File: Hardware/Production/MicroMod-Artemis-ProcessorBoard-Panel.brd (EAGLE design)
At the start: 244.6 x 83.1 mm, 766 parts, among them J1 MICROMOD-2222, J10 MICROMOD-2222, J11 MICROMOD-2222, J12 MICROMOD-2222, J13 MICROMOD-2222, J14 MICROMOD-2222, J15 MICROMOD-2222, J16 MICROMOD-2222, J17 MICROMOD-2222, J18 MICROMOD-2222, J19 MICROMOD-2222, J2 MICROMOD-2222, J20 MICROMOD-2222, J3 MICROMOD-2222, J4 MICROMOD-2222, J5 MICROMOD-2222, J6 MICROMOD-2222, J7 MICROMOD-2222, J8 MICROMOD-2222, J9 MICROMOD-2222, U1 ARTEMIS_MODULESMD, U10 ARTEMIS_MODULESMD, U11 CH340E_MSOP10, U12 TSV524, U13 ARTEMIS_MODULESMD, U14 CH340E_MSOP10, U15 TSV524, U16 ARTEMIS_MODULESMD, U17 CH340E_MSOP10, U18 TSV524, U19 ARTEMIS_MODULESMD, U2 TSV524, U20 CH340E_MSOP10, U21 TSV524, U22 ARTEMIS_MODULESMD, U23 CH340E_MSOP10, U24 TSV524, U25 ARTEMIS_MODULESMD, U26 CH340E_MSOP10, U27 TSV524, U28 ARTEMIS_MODULESMD, U29 CH340E_MSOP10, U3 ARTEMIS_MODULESMD, U30 TSV524, U31 ARTEMIS_MODULESMD, U32 CH340E_MSOP10, U33 TSV524, U34 ARTEMIS_MODULESMD, U35 CH340E_MSOP10, U36 TSV524, U37 ARTEMIS_MODULESMD, U38 CH340E_MSOP10, U39 TSV524, U4 CH340E_MSOP10, U40 ARTEMIS_MODULESMD, U41 CH340E_MSOP10, U42 TSV524, U43 ARTEMIS_MODULESMD, U44 CH340E_MSOP10, U45 TSV524, U46 ARTEMIS_MODULESMD, U47 CH340E_MSOP10, U48 TSV524, U49 ARTEMIS_MODULESMD, U5 TSV524, U50 CH340E_MSOP10, U51 TSV524, U52 ARTEMIS_MODULESMD, U53 CH340E_MSOP10, U54 TSV524, U55 ARTEMIS_MODULESMD, U56 CH340E_MSOP10, U57 TSV524, U58 ARTEMIS_MODULESMD, U59 CH340E_MSOP10, U6 CH340E_MSOP10, U60 TSV524, U7 ARTEMIS_MODULESMD, U8 CH340E_MSOP10, U9 TSV524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

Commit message: Adding v13 production files
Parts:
- removed C129, C130, C137, C138, C145, C146, C153, C154: 15pF, SparkFun-Capacitors:0402-TIGHT
- removed C131, C139, C147, C155: 10nF, SparkFun-Capacitors:0402-TIGHT
- removed C132, C133, C134, C136, C140, C141, C142, C144, C148, C149, C150, C152, C156, C157, C158, C160: 0.1uF, SparkFun-Capacitors:0402-TIGHT
- removed C135, C143, C151, C159: 1.0nF, SparkFun-Capacitors:0402-TIGHT
- removed D33, D35, D37, D39: BLUE, SparkFun-LED:LED-0603
- removed D34, D36, D38, D40: 1A/23V/620mV, SparkFun-DiscreteSemi:SOD-323
- removed FD65, FD66, FD67, FD68, FD69, FD70, FD71, FD72, FD73, FD74, FD75, FD76, FD77, FD78, FD79, FD80: FIDUCIALUFIDUCIAL, SparkFun-Aesthetics:FIDUCIAL-MICRO
- removed J17, J18, J19, J20: MICROMOD-2222, SparkFun-MicroMod:M.2-CARD-E-22
- removed LOGO49, LOGO52, LOGO55, LOGO58: OSHW-LOGOMINI, SparkFun-Aesthetics:OSHW-LOGO-MINI
- removed LOGO50, LOGO53, LOGO56, LOGO59: SFE_LOGO_NAME_FLAME.1_INCH, SparkFun-Aesthetics:SFE_LOGO_NAME_FLAME_.1
- removed LOGO51, LOGO54, LOGO57, LOGO60: SFE_LOGO_FLAME.1_INCH, SparkFun-Aesthetics:SFE_LOGO_FLAME_.1
- removed R145, R154, R163, R172: 1k, SparkFun-Resistors:0402-TIGHT
- removed R146, R148, R150, R152, R155, R157, R159, R161, R164, R166, R168, R170, R173, R175, R177, R179: 100k, SparkFun-Resistors:0402-TIGHT
- removed R147, R156, R165, R174: 220KOHM-0402T-1/16W-1%, SparkFun-Resistors:0402-TIGHT
- removed R149, R151, R153, R158, R160, R162, R167, R169, R171, R176, R178, R180: 150k, SparkFun-Resistors:0402-TIGHT
- removed U$113, U$120, U$127, U$134: (no value), buzzard_labels:ARTEMIS0
- removed U$114, U$121, U$128, U$135: (no value), buzzard_labels:MICROMOD1
- removed U$115, U$122, U$129, U$136: (no value), buzzard_labels (1):ARTEMIS2
- removed U$116, U$123, U$130, U$137: (no value), SparkFun-Buzzard:STAT_TO_32
- removed U$117, U$119, U$124, U$126, U$131, U$133, U$138, U$140: (no value), SparkFun-MicroMod:MICROMOD_MI_LOGO_.35
- removed U$118, U$125, U$132, U$139: (no value), SparkFun-MicroMod:MICROMOD_LOGO_.35
- removed U49, U52, U55, U58: ARTEMIS_MODULESMD, SparkFun-IC-Microcontroller:ARTEMIS_FP
- removed U50, U53, U56, U59: CH340E_MSOP10, SparkFun-IC-Comms:MSOP10
- removed U51, U54, U57, U60: TSV524, OpAmp:QFN-16
- removed Y17, Y18, Y19, Y20: 32.768kHz, SparkFun-Clocks:CRYSTAL-SMD-3.2X1.5MM
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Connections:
- removed net !RESET!16: C133.2, C135.1, J17.6, R146.1, U49.~RST
- removed net !RESET!17: C141.2, C143.1, J18.6, R155.1, U52.~RST
- removed net !RESET!18: C149.2, C151.1, J19.6, R164.1, U55.~RST
- removed net !RESET!19: C157.2, C159.1, J20.6, R173.1, U58.~RST
- removed net !RTS16: C133.1, C134.1, U50.4
- removed net !RTS17: C141.1, C142.1, U53.4
- removed net !RTS18: C149.1, C150.1, U56.4
- removed net !RTS19: C157.1, C158.1, U59.4
- removed net 3.3V16: C131.1, C132.1, C136.1, D34.C, J17.72, R146.2, U49.VDD@36, U49.VDD@37, U50.10, U50.7, U51.2
- removed net 3.3V17: C139.1, C140.1, C144.1, D36.C, J18.72, R155.2, U52.VDD@36, U52.VDD@37, U53.10, U53.7, U54.2
- removed net 3.3V18: C147.1, C148.1, C152.1, D38.C, J19.72, R164.2, U55.VDD@36, U55.VDD@37, U56.10, U56.7, U57.2
- removed net 3.3V19: C155.1, C156.1, C160.1, D40.C, J20.72, R173.2, U58.VDD@36, U58.VDD@37, U59.10, U59.7, U60.2
- removed net 3.3V_EN16: J17.4, U49.D3
- removed net 3.3V_EN17: J18.4, U52.D3
- removed net 3.3V_EN18: J19.4, U55.D3
- removed net 3.3V_EN19: J20.4, U58.D3
- removed net 3.3V_MAIN16: D34.A, J17.2, J17.74
- removed net 3.3V_MAIN17: D36.A, J18.2, J18.74
- removed net 3.3V_MAIN18: D38.A, J19.2, J19.74
- removed net 3.3V_MAIN19: D40.A, J20.2, J20.74
- removed net ADC0_BUFF33: R150.1, R151.2, U51.4
- removed net ADC0_BUFF34: R150.2, U51.15, U51.16
- removed net ADC0_BUFF35: R159.1, R160.2, U54.4
- removed net ADC0_BUFF36: R159.2, U54.15, U54.16
- removed net ADC0_BUFF37: R168.1, R169.2, U57.4
- removed net ADC0_BUFF38: R168.2, U57.15, U57.16
- removed net ADC0_BUFF39: R177.1, R178.2, U60.4
- removed net ADC0_BUFF40: R177.2, U60.15, U60.16
- removed net ADC1_BUFF17: R152.1, R153.2, U51.9
- removed net ADC1_BUFF18: R161.1, R162.2, U54.9
- removed net ADC1_BUFF19: R170.1, R171.2, U57.9
- removed net ADC1_BUFF20: R179.1, R180.2, U60.9
- removed net ADC32: J17.34, U51.1
- removed net ADC33: J17.38, U51.12
- removed net ADC34: J18.34, U54.1
- removed net ADC35: J18.38, U54.12
- removed net ADC36: J19.34, U57.1
- removed net ADC37: J19.38, U57.12
- removed net ADC38: J20.34, U60.1
- removed net ADC39: J20.38, U60.12
- removed net ADC_BUFF17: R152.2, U51.13, U51.14
- removed net ADC_BUFF18: R161.2, U54.13, U54.14
- removed net ADC_BUFF19: R170.2, U57.13, U57.14
- removed net ADC_BUFF20: R179.2, U60.13, U60.14
- removed net ADC_D+16: J17.63, U49.~AD13
- removed net ADC_D+17: J18.63, U52.~AD13
- removed net ADC_D+18: J19.63, U55.~AD13
- removed net ADC_D+19: J20.63, U58.~AD13
- removed net ADC_D-16: J17.65, U49.~AD12
- removed net ADC_D-17: J18.65, U52.~AD12
- removed net ADC_D-18: J19.65, U55.~AD12
- removed net ADC_D-19: J20.65, U58.~AD12
- removed net BATT_VIN/17: J17.51, R148.2
- removed net BATT_VIN/18: J18.51, R157.2
- removed net BATT_VIN/19: J19.51, R166.2
- removed net BATT_VIN/20: J20.51, R175.2
- removed net BOOT16: C134.2, J17.11, R147.2, U49.BOOT
- removed net BOOT17: C142.2, J18.11, R156.2, U52.BOOT
- removed net BOOT18: C150.2, J19.11, R165.2, U55.BOOT
- removed net BOOT19: C158.2, J20.11, R174.2, U58.BOOT
- removed net CAM_PCLK16: J17.54, U49.~AD11
- removed net CAM_PCLK17: J18.54, U52.~AD11
- removed net CAM_PCLK18: J19.54, U55.~AD11
- removed net CAM_PCLK19: J20.54, U58.~AD11
- removed net CLKOUT16: J17.56, J17.58, U49.D0
- removed net CLKOUT17: J18.56, J18.58, U52.D0
- removed net CLKOUT18: J19.56, J19.58, U55.D0
- removed net CLKOUT19: J20.56, J20.58, U58.D0
- removed net CTS17: J17.15, U49.D17
- removed net CTS18: J18.15, U52.D17
- removed net CTS19: J19.15, U55.D17
- removed net CTS20: J20.15, U58.D17
- removed net D32: J17.10, U49.D1
- removed net D33: J17.18, U49.D2
- removed net D34: J18.10, U52.D1
- removed net D35: J18.18, U52.D2
- removed net D36: J19.10, U55.D1
- removed net D37: J19.18, U55.D2
- removed net D38: J20.10, U58.D1
- removed net D39: J20.18, U58.D2
- removed net GND16: C129.1, C130.1, C131.2, C132.2, C135.2, C136.2, D33.C, J17.1, J17.33, J17.36, J17.39, J17.45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
- removed net GND17: C137.1, C138.1, C139.2, C140.2, C143.2, C144.2, D35.C, J18.1, J18.33, J18.36, J18.39, J18.45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
- removed net GND18: C145.1, C146.1, C147.2, C148.2, C151.2, C152.2, D37.C, J19.1, J19.33, J19.36, J19.39, J19.45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
- removed net GND19: C153.1, C154.1, C155.2, C156.2, C159.2, C160.2, D39.C, J20.1, J20.33, J20.36, J20.39, J20.45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
- removed net GPIO128: J17.73, U49.~AD29
- removed net GPIO129: J17.69, U49.D15
- removed net GPIO130: J17.71, U49.D14
- removed net GPIO131: J17.42, U49.~AD33/SWO
- removed net GPIO132: J17.46, U49.~D27
- removed net GPIO133: J17.44, U49.AD34
- removed net GPIO134: J17.48, U49.~D28
- removed net GPIO135: J17.40, U49.AD16
- removed net GPIO136: J18.73, U52.~AD29
- removed net GPIO137: J18.69, U52.D15
- removed net GPIO138: J18.71, U52.D14
- removed net GPIO139: J18.42, U52.~AD33/SWO
- removed net GPIO140: J18.46, U52.~D27
- removed net GPIO141: J18.44, U52.AD34
- removed net GPIO142: J18.48, U52.~D28
- removed net GPIO143: J18.40, U52.AD16
- removed net GPIO144: J19.73, U55.~AD29
- removed net GPIO145: J19.69, U55.D15
- removed net GPIO146: J19.71, U55.D14
- removed net GPIO147: J19.42, U55.~AD33/SWO
- removed net GPIO148: J19.46, U55.~D27
- removed net GPIO149: J19.44, U55.AD34
- removed net GPIO150: J19.48, U55.~D28
- removed net GPIO151: J19.40, U55.AD16
- removed net GPIO152: J20.73, U58.~AD29
- removed net GPIO153: J20.69, U58.D15
- removed net GPIO154: J20.71, U58.D14
- removed net GPIO155: J20.42, U58.~AD33/SWO
- removed net GPIO156: J20.46, U58.~D27
- removed net GPIO157: J20.44, U58.AD34
- removed net GPIO158: J20.48, U58.~D28
- removed net GPIO159: J20.40, U58.AD16
- removed net I2C_!INT!16: J17.16, U49.~D18
- removed net I2C_!INT!17: J18.16, U52.~D18
- removed net I2C_!INT!18: J19.16, U55.~D18
- removed net I2C_!INT!19: J20.16, U58.~D18
- removed net LED_BUILTIN16: R145.2, U49.~D19
- removed net LED_BUILTIN17: R154.2, U52.~D19
- removed net LED_BUILTIN18: R163.2, U55.~D19
- removed net LED_BUILTIN19: R172.2, U58.~D19
- removed net N$11 (its old number): U7.XI
- removed net N$16 (its old number): C25.2, Y4.P$1
- removed net N$19 (its old number): U13.XI
- removed net N$20 (its old number): C34.2, Y5.P$1
- removed net N$23 (its old number): U16.XI
- removed net N$28 (its old number): C50.2, Y7.P$1
- removed net N$31 (its old number): U22.XI
- removed net N$32 (its old number): C58.2, Y8.P$1
- removed net N$35 (its old number): U25.XI
- removed net N$40 (its old number): C74.2, Y10.P$1
- removed net N$43 (its old number): U31.XI
- removed net N$44 (its old number): C82.2, Y11.P$1
- removed net N$47 (its old number): U34.XI
- removed net N$51: U37.XI
- removed net N$52: C98.2, Y13.P$1
- removed net N$55: U40.XI
- removed net N$56: C106.2, Y14.P$1
- removed net N$59: U43.XI
- removed net N$6 (its old number): U3.XI
- removed net N$60: C114.2, Y15.P$1
- removed net N$63: U46.XI
- removed net N$64: C122.2, Y16.P$1
- removed net N$65: C129.2, U49.XO, Y17.P$2
- removed net N$66: D33.A, R145.1
- removed net N$67: U49.XI
- removed net N$68: C130.2, Y17.P$1
- removed net N$69: C137.2, U52.XO, Y18.P$2
- removed net N$70: D35.A, R154.1
- removed net N$71: U52.XI
- removed net N$72: C138.2, Y18.P$1
- removed net N$73: C145.2, U55.XO, Y19.P$2
- removed net N$74: D37.A, R163.1
- removed net N$75: U55.XI
- removed net N$76: C146.2, Y19.P$1
- removed net N$77: C153.2, U58.XO, Y20.P$2
- removed net N$78: D39.A, R172.1
- removed net N$79: U58.XI
- removed net N$8 (its old number): C3.2, Y2.P$1
- removed net N$80: C154.2, Y20.P$1
- removed net PDM_CLK16: J17.50, U49.~D37
- removed net PDM_CLK17: J18.50, U52.~D37
- removed net PDM_CLK18: J19.50, U55.~D37
- removed net PDM_CLK19: J20.50, U58.~D37
- removed net PDM_DATA16: J17.52, U49.D36
- removed net PDM_DATA17: J18.52, U52.D36
- removed net PDM_DATA18: J19.52, U55.D36
- removed net PDM_DATA19: J20.52, U58.D36
- removed net PWM32: J17.32, U49.~D44
- removed net PWM33: J17.47, U49.~D45
- removed net PWM34: J18.32, U52.~D44
- removed net PWM35: J18.47, U52.~D45
- removed net PWM36: J19.32, U55.~D44
- removed net PWM37: J19.47, U55.~D45
- removed net PWM38: J20.32, U58.~D44
- removed net PWM39: J20.47, U58.~D45
- removed net RTS17: J17.13, U49.D10
- removed net RTS18: J18.13, U52.D10
- removed net RTS19: J19.13, U55.D10
- removed net RTS20: J20.13, U58.D10
- removed net RX17: J17.19, U49.~D25
- removed net RX18: J18.19, U52.~D25
- removed net RX19: J19.19, U55.~D25
- removed net RX20: J20.19, U58.~D25
- removed net RXI-16: U49.RXI-0, U50.8
- removed net RXI-17: U52.RXI-0, U53.8
- removed net RXI-18: U55.RXI-0, U56.8
- removed net RXI-19: U58.RXI-0, U59.8
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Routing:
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- removed copper zone on layer 15, net 3.3V16
- removed copper zone on layer 15, net 3.3V17
- removed copper zone on layer 15, net 3.3V18
- removed copper zone on layer 15, net 3.3V19
- removed copper zone on layer 1, net GND16
- removed copper zone on layer 15, net GND16
- removed copper zone on layer 16, net GND16
- removed copper zone on layer 2, net GND16
- removed copper zone on layer 1, net GND17
- removed copper zone on layer 15, net GND17
- removed copper zone on layer 16, net GND17
- removed copper zone on layer 2, net GND17
- removed copper zone on layer 1, net GND18
- removed copper zone on layer 15, net GND18
- removed copper zone on layer 16, net GND18
- removed copper zone on layer 2, net GND18
- removed copper zone on layer 1, net GND19
- removed copper zone on layer 15, net GND19
- removed copper zone on layer 16, net GND19
- removed copper zone on layer 2, net GND19
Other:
- board size 244.6 x 83.1 mm -> 199.6 x 83.1 mm
- board text added: "v13"
- board text removed: "v12"

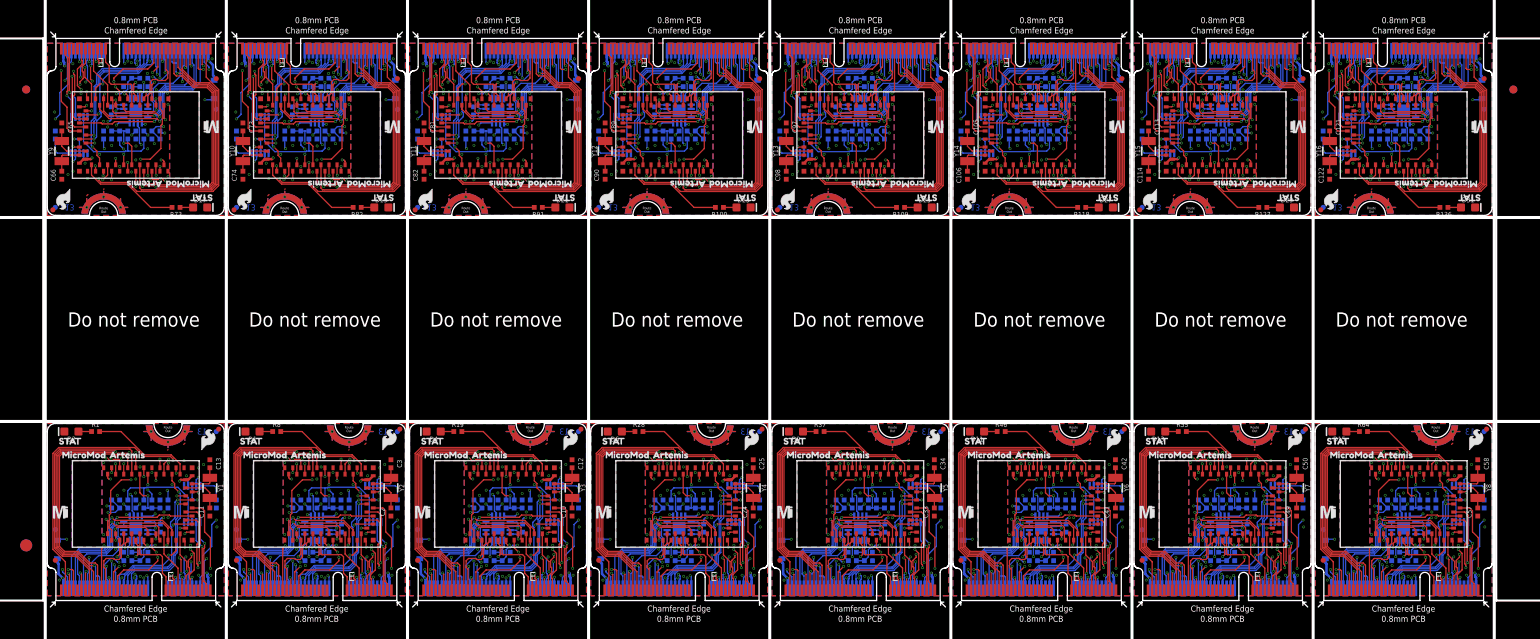
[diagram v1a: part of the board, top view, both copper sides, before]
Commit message: Adding additional decoupling, change version to v16.
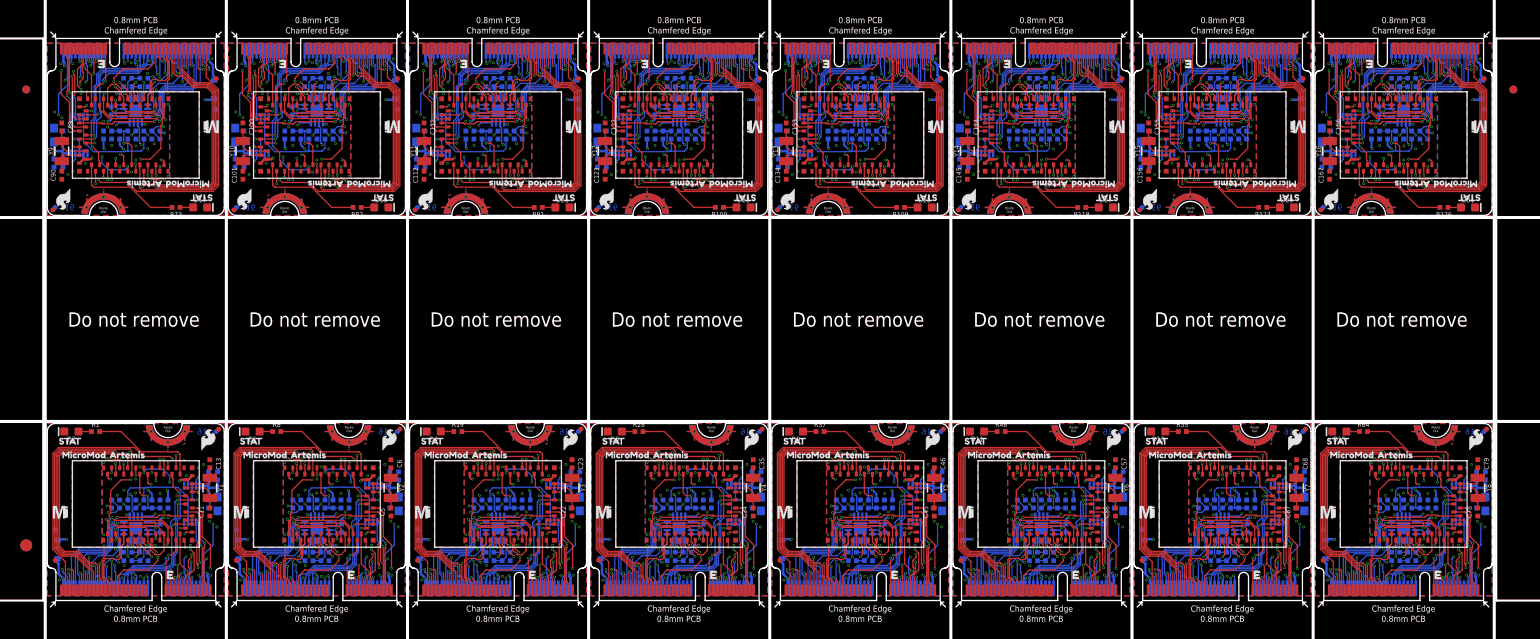
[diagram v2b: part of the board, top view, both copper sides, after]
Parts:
- added C129, C136, C137, C138, C140, C147, C148, C149, C151, C158, C159, C160, C162, C169, C170, C171, C173: 0.1uF, SparkFun-Capacitors:0402-TIGHT
- added C130, C141, C152, C163, C174: 0.22uF, SparkFun-Capacitors:0402-TIGHT
- added C131, C142, C153, C164, C175: 1.0uF, SparkFun-Capacitors:0402-TIGHT
- added C132, C143, C154, C165, C176: 10uF, SparkFun-Capacitors:0603
- added C133, C134, C144, C145, C155, C156, C166, C167: 15pF, SparkFun-Capacitors:0402-TIGHT
- added C135, C146, C157, C168: 10nF, SparkFun-Capacitors:0402-TIGHT
- added C139, C150, C161, C172: 1.0nF, SparkFun-Capacitors:0402-TIGHT
- C10, C105, C114, C25, C41, C49, C50, C74, C81, C82: value 15pF -> 0.1uF
- C100, C101, C112, C23, C45, C46, C5, C56, C6, C68, C78: value 0.1uF -> 15pF
- C102, C124, C36, C69, C7, C80: value 0.1uF -> 10nF
- C103, C127, C39, C63, C71, C8: value 1.0nF -> 0.1uF
- C106, C12, C73: value 15pF -> 1.0nF
- C107, C115, C14, C26, C59, C83: value 10nF -> 0.1uF
- C108, C15, C53, C64, C86: value 0.1uF -> 0.22uF
- C109, C120, C16, C32, C54, C76: value 0.1uF -> 1.0uF
- C110, C19, C44, C77, C88: value 0.1uF -> 10uF; device SparkFun-Capacitors:0402-TIGHT -> SparkFun-Capacitors:0603
- C111, C22, C79: value 1.0nF -> 15pF
- C113, C24, C58: value 15pF -> 10nF
- C117, C128, C29, C40, C62, C84: value 0.1uF -> 1.0nF
- C119, C31: value 1.0nF -> 0.22uF
- C121, C33, C66: value 15pF -> 10uF; device SparkFun-Capacitors:0402-TIGHT -> SparkFun-Capacitors:0603
- C123, C35, C67: value 10nF -> 15pF
- C2, C42, C97: value 15pF -> 0.22uF
- C3, C65, C98: value 15pF -> 1.0uF
- C4, C99: value 10nF -> 10uF; device SparkFun-Capacitors:0402-TIGHT -> SparkFun-Capacitors:0603
- C43: value 10nF -> 1.0uF
- C47: value 1.0nF -> 10nF
- C51: value 10nF -> 1.0nF
- C55: value 1.0nF -> 10uF; device SparkFun-Capacitors:0402-TIGHT -> SparkFun-Capacitors:0603
- C75: value 10nF -> 0.22uF
- C87: value 1.0nF -> 1.0uF
- R10, R102, R111, R120, R129, R138, R15, R21, R30, R39, R48, R57, R66, R75, R84, R93: value 220KOHM-0402T-1/16W-1% -> 220K
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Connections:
- net SDIO_DATA1 renamed QSPI1
- net SDIO_DATA10 renamed QSPI10
- net SDIO_DATA11 renamed QSPI11
- net SDIO_DATA12 renamed QSPI12
- net SDIO_DATA13 renamed QSPI13
- net SDIO_DATA14 renamed QSPI14
- net SDIO_DATA15 renamed QSPI15
- net SDIO_DATA16 renamed QSPI16
- net SDIO_DATA17 renamed QSPI17
- net SDIO_DATA18 renamed QSPI18
- net SDIO_DATA19 renamed QSPI19
- net SDIO_DATA2 renamed QSPI2
- net SDIO_DATA20 renamed QSPI20
- net SDIO_DATA21 renamed QSPI21
- net SDIO_DATA22 renamed QSPI22
- net SDIO_DATA23 renamed QSPI23
- net SDIO_DATA24 renamed QSPI24
- net SDIO_DATA25 renamed QSPI25
- net SDIO_DATA26 renamed QSPI26
- net SDIO_DATA27 renamed QSPI27
- net SDIO_DATA28 renamed QSPI28
- net SDIO_DATA29 renamed QSPI29
- net SDIO_DATA3 renamed QSPI3
- net SDIO_DATA30 renamed QSPI30
- net SDIO_DATA31 renamed QSPI31
- net SDIO_DATA32 renamed QSPI32
- net SDIO_DATA4 renamed QSPI4
- net SDIO_DATA5 renamed QSPI5
- net SDIO_DATA6 renamed QSPI6
- net SDIO_DATA7 renamed QSPI7
- net SDIO_DATA8 renamed QSPI8
- net SDIO_DATA9 renamed QSPI9
- net SPI_!CS! renamed SPI_!CS!/QSPI3
- net SPI_!CS!18 renamed SPI_!CS!/QSPI10
- net SPI_!CS!20 renamed SPI_!CS!/QSPI11
- net SPI_!CS!22 renamed SPI_!CS!/QSPI12
- net SPI_!CS!24 renamed SPI_!CS!/QSPI13
- net SPI_!CS!26 renamed SPI_!CS!/QSPI14
- net SPI_!CS!28 renamed SPI_!CS!/QSPI15
- net SPI_!CS!30 renamed SPI_!CS!/QSPI16
- net SPI_MISO renamed SPI_MISO/QSPI0
- net SPI_MISO18 renamed SPI_MISO/QSPI9
- net SPI_MISO20 renamed SPI_MISO/QSPI10
- net SPI_MISO22 renamed SPI_MISO/QSPI11
- net SPI_MISO24 renamed SPI_MISO/QSPI12
- net SPI_MISO26 renamed SPI_MISO/QSPI13
- net SPI_MISO28 renamed SPI_MISO/QSPI14
- net SPI_MISO30 renamed SPI_MISO/QSPI15
- net SPI_MOSI renamed SPI_MOSI/QSPI_!CS!
- net SPI_MOSI17 renamed SPI_MOSI/QSPI_!CS!8
- net SPI_MOSI19 renamed SPI_MOSI/QSPI_!CS!9
- net SPI_MOSI21 renamed SPI_MOSI/QSPI_!CS!10
- net SPI_MOSI23 renamed SPI_MOSI/QSPI_!CS!11
- net SPI_MOSI25 renamed SPI_MOSI/QSPI_!CS!12
- net SPI_MOSI27 renamed SPI_MOSI/QSPI_!CS!13
- net SPI_MOSI29 renamed SPI_MOSI/QSPI_!CS!14
- net SPI_MOSI31 renamed SPI_MOSI/QSPI_!CS!15
- removed net ADC_D-: J1.65, U1.~AD12
- removed net ADC_D-1: J2.65, U3.~AD12
- removed net ADC_D-10: J11.65, U31.~AD12
- removed net ADC_D-11: J12.65, U34.~AD12
- removed net ADC_D-12: J13.65, U37.~AD12
- removed net ADC_D-13: J14.65, U40.~AD12
- removed net ADC_D-14: J15.65, U43.~AD12
- removed net ADC_D-15: J16.65, U46.~AD12
- removed net ADC_D-2: J3.65, U7.~AD12
- removed net ADC_D-3: J4.65, U10.~AD12
- removed net ADC_D-4: J5.65, U13.~AD12
- removed net ADC_D-5: J6.65, U16.~AD12
- removed net ADC_D-6: J7.65, U19.~AD12
- removed net ADC_D-7: J8.65, U22.~AD12
- removed net ADC_D-8: J9.65, U25.~AD12
- removed net ADC_D-9: J10.65, U28.~AD12
- removed net CLKOUT: J1.56, J1.58, U1.D0
- removed net CLKOUT1: J2.56, J2.58, U3.D0
- removed net CLKOUT10: J11.56, J11.58, U31.D0
- removed net CLKOUT11: J12.56, J12.58, U34.D0
- removed net CLKOUT12: J13.56, J13.58, U37.D0
- removed net CLKOUT13: J14.56, J14.58, U40.D0
- removed net CLKOUT14: J15.56, J15.58, U43.D0
- removed net CLKOUT15: J16.56, J16.58, U46.D0
- removed net CLKOUT2: J3.56, J3.58, U7.D0
- removed net CLKOUT3: J4.56, J4.58, U10.D0
- removed net CLKOUT4: J5.56, J5.58, U13.D0
- removed net CLKOUT5: J6.56, J6.58, U16.D0
- removed net CLKOUT6: J7.56, J7.58, U19.D0
- removed net CLKOUT7: J8.56, J8.58, U22.D0
- removed net CLKOUT8: J9.56, J9.58, U25.D0
- removed net CLKOUT9: J10.56, J10.58, U28.D0
- removed net SPI_!CS!17: J9.49, U25.D41
- removed net SPI_!CS!19: J10.49, U28.D41
- removed net SPI_!CS!21: J11.49, U31.D41
- removed net SPI_!CS!23: J12.49, U34.D41
- removed net SPI_!CS!25: J13.49, U37.D41
- removed net SPI_!CS!27: J14.49, U40.D41
- removed net SPI_!CS!29: J15.49, U43.D41
- removed net SPI_!CS!31: J16.49, U46.D41
- removed net SPI_MISO17: J9.61, U25.~D43
- removed net SPI_MISO19: J10.61, U28.~D43
- removed net SPI_MISO21: J11.61, U31.~D43
- removed net SPI_MISO23: J12.61, U34.~D43
- removed net SPI_MISO25: J13.61, U37.~D43
- removed net SPI_MISO27: J14.61, U40.~D43
- removed net SPI_MISO29: J15.61, U43.~D43
- removed net SPI_MISO31: J16.61, U46.~D43
- removed net SPI_MOSI18: J10.59, U28.D38
- removed net SPI_MOSI20: J11.59, U31.D38
- removed net SPI_MOSI22: J12.59, U34.D38
- removed net SPI_MOSI24: J13.59, U37.D38
- removed net SPI_MOSI26: J14.59, U40.D38
- removed net SPI_MOSI28: J15.59, U43.D38
- removed net SPI_MOSI30: J16.59, U46.D38
- removed net SPI_SCK: J1.60, U1.~D5
- removed net SPI_SCK17: J9.60, U25.~D5
- removed net SPI_SCK18: J10.57, U28.~D42
- removed net SPI_SCK19: J10.60, U28.~D5
- removed net SPI_SCK20: J11.57, U31.~D42
- removed net SPI_SCK21: J11.60, U31.~D5
- removed net SPI_SCK22: J12.57, U34.~D42
- removed net SPI_SCK23: J12.60, U34.~D5
- removed net SPI_SCK24: J13.57, U37.~D42
- removed net SPI_SCK25: J13.60, U37.~D5
- removed net SPI_SCK26: J14.57, U40.~D42
- removed net SPI_SCK27: J14.60, U40.~D5
- removed net SPI_SCK28: J15.57, U43.~D42
- removed net SPI_SCK29: J15.60, U43.~D5
- removed net SPI_SCK30: J16.57, U46.~D42
- removed net SPI_SCK31: J16.60, U46.~D5
- removed net TX1: J1.17, U1.~D24
- removed net TX10: J10.17, U28.~D24
- removed net TX11: J11.17, U31.~D24
- removed net TX12: J12.17, U34.~D24
- removed net TX13: J13.17, U37.~D24
- removed net TX14: J14.17, U40.~D24
- removed net TX15: J15.17, U43.~D24
- removed net TX16: J16.17, U46.~D24
- removed net TX2: J2.17, U3.~D24
- removed net TX3: J3.17, U7.~D24
- removed net TX4: J4.17, U10.~D24
- removed net TX5: J5.17, U13.~D24
- removed net TX6: J6.17, U16.~D24
- removed net TX7: J7.17, U19.~D24
- removed net TX8: J8.17, U22.~D24
- removed net TX9: J9.17, U25.~D24
- new net CAM_MCLK: J1.56, J1.58, U1.~D18
- new net CAM_MCLK1: J2.56, J2.58, U3.~D18
- new net CAM_MCLK10: J11.56, J11.58, U31.~D18
- new net CAM_MCLK11: J12.56, J12.58, U34.~D18
- new net CAM_MCLK12: J13.56, J13.58, U37.~D18
- new net CAM_MCLK13: J14.56, J14.58, U40.~D18
- new net CAM_MCLK14: J15.56, J15.58, U43.~D18
- new net CAM_MCLK15: J16.56, J16.58, U46.~D18
- new net CAM_MCLK2: J3.56, J3.58, U7.~D18
- new net CAM_MCLK3: J4.56, J4.58, U10.~D18
- new net CAM_MCLK4: J5.56, J5.58, U13.~D18
- new net CAM_MCLK5: J6.56, J6.58, U16.~D18
- new net CAM_MCLK6: J7.56, J7.58, U19.~D18
- new net CAM_MCLK7: J8.56, J8.58, U22.~D18
- new net CAM_MCLK8: J9.56, J9.58, U25.~D18
- new net CAM_MCLK9: J10.56, J10.58, U28.~D18
- new net SPI_!CS!/QSPI1: J2.70, U3.~D23
- new net SPI_!CS!/QSPI2: J3.70, U7.~D23
- new net SPI_!CS!/QSPI4: J4.70, U10.~D23
- new net SPI_!CS!/QSPI5: J5.70, U13.~D23
- new net SPI_!CS!/QSPI6: J6.70, U16.~D23
- new net SPI_!CS!/QSPI7: J7.70, U19.~D23
- new net SPI_!CS!/QSPI8: J8.70, U22.~D23
- new net SPI_!CS!/QSPI9: J9.70, U25.~D23
- new net SPI_MISO/QSPI1: J2.64, U3.~D22, U3.~D6
- new net SPI_MISO/QSPI2: J3.64, U7.~D22, U7.~D6
- new net SPI_MISO/QSPI3: J4.64, U10.~D22, U10.~D6
- new net SPI_MISO/QSPI4: J5.64, U13.~D22, U13.~D6
- new net SPI_MISO/QSPI5: J6.64, U16.~D22, U16.~D6
- new net SPI_MISO/QSPI6: J7.64, U19.~D22, U19.~D6
- new net SPI_MISO/QSPI7: J8.64, U22.~D22, U22.~D6
- new net SPI_MISO/QSPI8: J9.64, U25.~D22, U25.~D6
- new net SPI_MOSI/QSPI_!CS!1: J2.62, U3.D7
- new net SPI_MOSI/QSPI_!CS!2: J3.62, U7.D7
- new net SPI_MOSI/QSPI_!CS!3: J4.62, U10.D7
- new net SPI_MOSI/QSPI_!CS!4: J5.62, U13.D7
- new net SPI_MOSI/QSPI_!CS!5: J6.62, U16.D7
- new net SPI_MOSI/QSPI_!CS!6: J7.62, U19.D7
- new net SPI_MOSI/QSPI_!CS!7: J8.62, U22.D7
- new net SPI_SCK/QSPI_SCK: J1.60, U1.~D24, U1.~D5
- new net SPI_SCK/QSPI_SCK1: J2.60, U3.~D24, U3.~D5
- new net SPI_SCK/QSPI_SCK10: J11.60, U31.~D24, U31.~D5
- new net SPI_SCK/QSPI_SCK11: J12.60, U34.~D24, U34.~D5
- new net SPI_SCK/QSPI_SCK12: J13.60, U37.~D24, U37.~D5
- new net SPI_SCK/QSPI_SCK13: J14.60, U40.~D24, U40.~D5
- new net SPI_SCK/QSPI_SCK14: J15.60, U43.~D24, U43.~D5
- new net SPI_SCK/QSPI_SCK15: J16.60, U46.~D24, U46.~D5
- new net SPI_SCK/QSPI_SCK2: J3.60, U7.~D24, U7.~D5
- new net SPI_SCK/QSPI_SCK3: J4.60, U10.~D24, U10.~D5
- new net SPI_SCK/QSPI_SCK4: J5.60, U13.~D24, U13.~D5
- new net SPI_SCK/QSPI_SCK5: J6.60, U16.~D24, U16.~D5
- new net SPI_SCK/QSPI_SCK6: J7.60, U19.~D24, U19.~D5
- new net SPI_SCK/QSPI_SCK7: J8.60, U22.~D24, U22.~D5
- new net SPI_SCK/QSPI_SCK8: J9.60, U25.~D24, U25.~D5
- new net SPI_SCK/QSPI_SCK9: J10.60, U28.~D24, U28.~D5
- new net TX1/ADC_D-: J1.17, J1.65, U1.~AD12
- new net TX1/ADC_D-1: J2.17, J2.65, U3.~AD12
- new net TX1/ADC_D-10: J11.17, J11.65, U31.~AD12
- new net TX1/ADC_D-11: J12.17, J12.65, U34.~AD12
- new net TX1/ADC_D-12: J13.17, J13.65, U37.~AD12
- new net TX1/ADC_D-13: J14.17, J14.65, U40.~AD12
- new net TX1/ADC_D-14: J15.17, J15.65, U43.~AD12
- new net TX1/ADC_D-15: J16.17, J16.65, U46.~AD12
- new net TX1/ADC_D-2: J3.17, J3.65, U7.~AD12
- new net TX1/ADC_D-3: J4.17, J4.65, U10.~AD12
- new net TX1/ADC_D-4: J5.17, J5.65, U13.~AD12
- new net TX1/ADC_D-5: J6.17, J6.65, U16.~AD12
- new net TX1/ADC_D-6: J7.17, J7.65, U19.~AD12
- new net TX1/ADC_D-7: J8.17, J8.65, U22.~AD12
- new net TX1/ADC_D-8: J9.17, J9.65, U25.~AD12
- new net TX1/ADC_D-9: J10.17, J10.65, U28.~AD12
- net !RESET!1: now also C12.1, C9.2; no longer C6.2, C8.1
- net !RESET!10: now also C115.2, C117.1; no longer C85.2, C87.1
- net !RESET!11: now also C126.2, C128.1; no longer C93.2, C95.1
- net !RESET!12: now also C137.2, C139.1; no longer C101.2, C103.1
- net !RESET!13: now also C148.2, C150.1; no longer C109.2, C111.1
- net !RESET!14: now also C159.2, C161.1; no longer C117.2, C119.1
- net !RESET!15: now also C170.2, C172.1; no longer C125.2, C127.1
- net !RESET!2: now also C26.2, C29.1; no longer C16.2, C22.1
- net !RESET!3: now also C38.2, C40.1; no longer C29.2, C31.1
- net !RESET!4: now also C49.2, C51.1; no longer C37.2, C39.1
- net !RESET!5: now also C60.2, C62.1; no longer C45.2, C47.1
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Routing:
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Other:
- board text added: "v16"
- board text removed: "v13"

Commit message: Adding v17 production files
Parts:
- removed U$100, U$107: (no value), buzzard_labels:MICROMOD1
- removed U$101, U$108: (no value), buzzard_labels (1):ARTEMIS2
- removed U$102, U$109: (no value), SparkFun-Buzzard:STAT_TO_32
- removed U$103, U$105, U$110, U$112, U$98: (no value), SparkFun-MicroMod:MICROMOD_MI_LOGO_.35
- removed U$104, U$111, U$97: (no value), SparkFun-MicroMod:MICROMOD_LOGO_.35
- removed U$106, U$99: (no value), buzzard_labels:ARTEMIS0
- U$10, U$17, U$59: device buzzard_labels (1):ARTEMIS2 -> output:ARTEMIS0
- U$11, U$18, U$60: device SparkFun-Buzzard:STAT_TO_32 -> output:STAT0
- U$12, U$42, U$54, U$84, U$96: device SparkFun-MicroMod:MICROMOD_MI_LOGO_.35 -> output:STAT0
- U$13, U$27, U$55, U$69: device SparkFun-MicroMod:MICROMOD_LOGO_.35 -> SparkFun-MicroMod:MICROMOD_MI_LOGO_.35
- U$14, U$26, U$56, U$68: device SparkFun-MicroMod:MICROMOD_MI_LOGO_.35 -> SparkFun-MicroMod:MICROMOD_LOGO_.35
- U$15, U$2, U$43, U$57, U$85: device buzzard_labels:ARTEMIS0 -> SparkFun-MicroMod:MICROMOD_MI_LOGO_.35
- U$16, U$58: device buzzard_labels:MICROMOD1 -> output:MICROMOD_ARTEMIS0
- U$22, U$64, U$8: device buzzard_labels:ARTEMIS0 -> output:MICROMOD_ARTEMIS0
- U$23, U$65, U$9: device buzzard_labels:MICROMOD1 -> output:ARTEMIS0
- U$24, U$66: device buzzard_labels (1):ARTEMIS2 -> output:STAT0
- U$25, U$39, U$4, U$67, U$81: device SparkFun-Buzzard:STAT_TO_32 -> SparkFun-MicroMod:MICROMOD_MI_LOGO_.35
- U$28, U$40, U$70, U$82: device SparkFun-MicroMod:MICROMOD_MI_LOGO_.35 -> output:MICROMOD_ARTEMIS0
- U$29, U$71: device buzzard_labels:ARTEMIS0 -> output:ARTEMIS0
- U$3, U$44, U$86: device buzzard_labels:MICROMOD1 -> SparkFun-MicroMod:MICROMOD_LOGO_.35
- U$30, U$72: device buzzard_labels:MICROMOD1 -> output:STAT0
- U$31, U$45, U$73, U$87: device buzzard_labels (1):ARTEMIS2 -> SparkFun-MicroMod:MICROMOD_MI_LOGO_.35
- U$32, U$74: device SparkFun-Buzzard:STAT_TO_32 -> SparkFun-MicroMod:MICROMOD_LOGO_.35
- U$34, U$76: device SparkFun-MicroMod:MICROMOD_LOGO_.35 -> output:MICROMOD_ARTEMIS0
- U$35, U$47, U$77, U$89: device SparkFun-MicroMod:MICROMOD_MI_LOGO_.35 -> output:ARTEMIS0
- U$36, U$78: device buzzard_labels:ARTEMIS0 -> output:STAT0
- U$37, U$51, U$79, U$93: device buzzard_labels:MICROMOD1 -> SparkFun-MicroMod:MICROMOD_MI_LOGO_.35
- U$38, U$80: device buzzard_labels (1):ARTEMIS2 -> SparkFun-MicroMod:MICROMOD_LOGO_.35
- U$41, U$83: device SparkFun-MicroMod:MICROMOD_LOGO_.35 -> output:ARTEMIS0
- U$46, U$88: device SparkFun-Buzzard:STAT_TO_32 -> output:MICROMOD_ARTEMIS0
- U$48, U$90: device SparkFun-MicroMod:MICROMOD_LOGO_.35 -> output:STAT0
- U$50, U$92: device buzzard_labels:ARTEMIS0 -> SparkFun-MicroMod:MICROMOD_LOGO_.35
- U$52, U$6, U$94: device buzzard_labels (1):ARTEMIS2 -> output:MICROMOD_ARTEMIS0
- U$53, U$95: device SparkFun-Buzzard:STAT_TO_32 -> output:ARTEMIS0
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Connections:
- net SPI_!CS!/QSPI1 renamed SPI_!CS1!/QSPI1
- net SPI_!CS!/QSPI10 renamed SPI_!CS1!/QSPI10
- net SPI_!CS!/QSPI11 renamed SPI_!CS1!/QSPI11
- net SPI_!CS!/QSPI12 renamed SPI_!CS1!/QSPI12
- net SPI_!CS!/QSPI13 renamed SPI_!CS1!/QSPI13
- net SPI_!CS!/QSPI14 renamed SPI_!CS1!/QSPI14
- net SPI_!CS!/QSPI15 renamed SPI_!CS1!/QSPI15
- net SPI_!CS!/QSPI16 renamed SPI_!CS1!/QSPI16
- net SPI_!CS!/QSPI2 renamed SPI_!CS1!/QSPI2
- net SPI_!CS!/QSPI3 renamed SPI_!CS1!/QSPI3
- net SPI_!CS!/QSPI4 renamed SPI_!CS1!/QSPI4
- net SPI_!CS!/QSPI5 renamed SPI_!CS1!/QSPI5
- net SPI_!CS!/QSPI6 renamed SPI_!CS1!/QSPI6
- net SPI_!CS!/QSPI7 renamed SPI_!CS1!/QSPI7
- net SPI_!CS!/QSPI8 renamed SPI_!CS1!/QSPI8
- net SPI_!CS!/QSPI9 renamed SPI_!CS1!/QSPI9
- net SPI_MISO/QSPI0 renamed SPI_CIPO1/QSPI0
- net SPI_MISO/QSPI1 renamed SPI_CIPO1/QSPI1
- net SPI_MISO/QSPI10 renamed SPI_CIPO1/QSPI10
- net SPI_MISO/QSPI11 renamed SPI_CIPO1/QSPI11
- net SPI_MISO/QSPI12 renamed SPI_CIPO1/QSPI12
- net SPI_MISO/QSPI13 renamed SPI_CIPO1/QSPI13
- net SPI_MISO/QSPI14 renamed SPI_CIPO1/QSPI14
- net SPI_MISO/QSPI15 renamed SPI_CIPO1/QSPI15
- net SPI_MISO/QSPI2 renamed SPI_CIPO1/QSPI2
- net SPI_MISO/QSPI3 renamed SPI_CIPO1/QSPI3
- net SPI_MISO/QSPI4 renamed SPI_CIPO1/QSPI4
- net SPI_MISO/QSPI5 renamed SPI_CIPO1/QSPI5
- net SPI_MISO/QSPI6 renamed SPI_CIPO1/QSPI6
- net SPI_MISO/QSPI7 renamed SPI_CIPO1/QSPI7
- net SPI_MISO/QSPI8 renamed SPI_CIPO1/QSPI8
- net SPI_MISO/QSPI9 renamed SPI_CIPO1/QSPI9
- net SPI_MISO1 renamed SPI_CIPO
- net SPI_MISO10 renamed SPI_CIPO9
- net SPI_MISO11 renamed SPI_CIPO10
- net SPI_MISO12 renamed SPI_CIPO11
- net SPI_MISO13 renamed SPI_CIPO12
- net SPI_MISO14 renamed SPI_CIPO13
- net SPI_MISO15 renamed SPI_CIPO14
- net SPI_MISO16 renamed SPI_CIPO15
- net SPI_MISO2 renamed SPI_CIPO1
- net SPI_MISO3 renamed SPI_CIPO2
- net SPI_MISO4 renamed SPI_CIPO3
- net SPI_MISO5 renamed SPI_CIPO4
- net SPI_MISO6 renamed SPI_CIPO5
- net SPI_MISO7 renamed SPI_CIPO6
- net SPI_MISO8 renamed SPI_CIPO7
- net SPI_MISO9 renamed SPI_CIPO8
- net SPI_MOSI/QSPI_!CS! renamed SPI_COPI1/QSPI_!CS!
- net SPI_MOSI/QSPI_!CS!1 renamed SPI_COPI1/QSPI_!CS!1
- net SPI_MOSI/QSPI_!CS!10 renamed SPI_COPI1/QSPI_!CS!10
- net SPI_MOSI/QSPI_!CS!11 renamed SPI_COPI1/QSPI_!CS!11
- net SPI_MOSI/QSPI_!CS!12 renamed SPI_COPI1/QSPI_!CS!12
- net SPI_MOSI/QSPI_!CS!13 renamed SPI_COPI1/QSPI_!CS!13
- net SPI_MOSI/QSPI_!CS!14 renamed SPI_COPI1/QSPI_!CS!14
- net SPI_MOSI/QSPI_!CS!15 renamed SPI_COPI1/QSPI_!CS!15
- net SPI_MOSI/QSPI_!CS!2 renamed SPI_COPI1/QSPI_!CS!2
- net SPI_MOSI/QSPI_!CS!3 renamed SPI_COPI1/QSPI_!CS!3
- net SPI_MOSI/QSPI_!CS!4 renamed SPI_COPI1/QSPI_!CS!4
- net SPI_MOSI/QSPI_!CS!5 renamed SPI_COPI1/QSPI_!CS!5
- net SPI_MOSI/QSPI_!CS!6 renamed SPI_COPI1/QSPI_!CS!6
- net SPI_MOSI/QSPI_!CS!7 renamed SPI_COPI1/QSPI_!CS!7
- net SPI_MOSI/QSPI_!CS!8 renamed SPI_COPI1/QSPI_!CS!8
- net SPI_MOSI/QSPI_!CS!9 renamed SPI_COPI1/QSPI_!CS!9
- net SPI_MOSI1 renamed SPI_COPI
- net SPI_MOSI10 renamed SPI_COPI9
- net SPI_MOSI11 renamed SPI_COPI10
- net SPI_MOSI12 renamed SPI_COPI11
- net SPI_MOSI13 renamed SPI_COPI12
- net SPI_MOSI14 renamed SPI_COPI13
- net SPI_MOSI15 renamed SPI_COPI14
- net SPI_MOSI16 renamed SPI_COPI15
- net SPI_MOSI2 renamed SPI_COPI1
- net SPI_MOSI3 renamed SPI_COPI2
- net SPI_MOSI4 renamed SPI_COPI3
- net SPI_MOSI5 renamed SPI_COPI4
- net SPI_MOSI6 renamed SPI_COPI5
- net SPI_MOSI7 renamed SPI_COPI6
- net SPI_MOSI8 renamed SPI_COPI7
- net SPI_MOSI9 renamed SPI_COPI8
- net SPI_SCK/QSPI_SCK renamed SPI_SCK1/QSPI_SCK
- net SPI_SCK/QSPI_SCK1 renamed SPI_SCK1/QSPI_SCK1
- net SPI_SCK/QSPI_SCK10 renamed SPI_SCK1/QSPI_SCK10
- net SPI_SCK/QSPI_SCK11 renamed SPI_SCK1/QSPI_SCK11
- net SPI_SCK/QSPI_SCK12 renamed SPI_SCK1/QSPI_SCK12
- net SPI_SCK/QSPI_SCK13 renamed SPI_SCK1/QSPI_SCK13
- net SPI_SCK/QSPI_SCK14 renamed SPI_SCK1/QSPI_SCK14
- net SPI_SCK/QSPI_SCK15 renamed SPI_SCK1/QSPI_SCK15
- net SPI_SCK/QSPI_SCK2 renamed SPI_SCK1/QSPI_SCK2
- net SPI_SCK/QSPI_SCK3 renamed SPI_SCK1/QSPI_SCK3
- net SPI_SCK/QSPI_SCK4 renamed SPI_SCK1/QSPI_SCK4
- net SPI_SCK/QSPI_SCK5 renamed SPI_SCK1/QSPI_SCK5
- net SPI_SCK/QSPI_SCK6 renamed SPI_SCK1/QSPI_SCK6
- net SPI_SCK/QSPI_SCK7 renamed SPI_SCK1/QSPI_SCK7
- net SPI_SCK/QSPI_SCK8 renamed SPI_SCK1/QSPI_SCK8
- net SPI_SCK/QSPI_SCK9 renamed SPI_SCK1/QSPI_SCK9
- removed net 3.3V_MAIN: D7.A, J1.2, J1.74
- removed net 3.3V_MAIN1: D3.A, J2.2, J2.74
- removed net 3.3V_MAIN10: D22.A, J11.2, J11.74
- removed net 3.3V_MAIN11: D24.A, J12.2, J12.74
- removed net 3.3V_MAIN12: D26.A, J13.2, J13.74
- removed net 3.3V_MAIN13: D28.A, J14.2, J14.74
- removed net 3.3V_MAIN14: D30.A, J15.2, J15.74
- removed net 3.3V_MAIN15: D32.A, J16.2, J16.74
- removed net 3.3V_MAIN2: D5.A, J3.2, J3.74
- removed net 3.3V_MAIN3: D8.A, J4.2, J4.74
- removed net 3.3V_MAIN4: D10.A, J5.2, J5.74
- removed net 3.3V_MAIN5: D12.A, J6.2, J6.74
- removed net 3.3V_MAIN6: D14.A, J7.2, J7.74
- removed net 3.3V_MAIN7: D16.A, J8.2, J8.74
- removed net 3.3V_MAIN8: D18.A, J9.2, J9.74
- removed net 3.3V_MAIN9: D20.A, J10.2, J10.74
- removed net SPI_!CS!16: J16.55, U46.D41
- removed net SPI_SCK16: J16.57, U46.~D42
- new net SPI_!CS!: J1.55, U1.D41
- new net SPI_SCK: J1.57, U1.~D42
- new net V_BATT: C1.1, C3.1, C4.1, D7.C, J1.72, R14.2, U1.VDD@36, U1.VDD@37, U2.2
- new net V_BATT1: C14.1, C16.1, C19.1, D3.C, J2.72, R9.2, U3.VDD@36, U3.VDD@37, U5.2
- new net V_BATT10: C118.1, C120.1, C121.1, D22.C, J11.72, R92.2, U31.VDD@36, U31.VDD@37, U33.2
- new net V_BATT11: C129.1, C131.1, C132.1, D24.C, J12.72, R101.2, U34.VDD@36, U34.VDD@37, U36.2
- new net V_BATT12: C140.1, C142.1, C143.1, D26.C, J13.72, R110.2, U37.VDD@36, U37.VDD@37, U39.2
- new net V_BATT13: C151.1, C153.1, C154.1, D28.C, J14.72, R119.2, U40.VDD@36, U40.VDD@37, U42.2
- new net V_BATT14: C162.1, C164.1, C165.1, D30.C, J15.72, R128.2, U43.VDD@36, U43.VDD@37, U45.2
- new net V_BATT15: C173.1, C175.1, C176.1, D32.C, J16.72, R137.2, U46.VDD@36, U46.VDD@37, U48.2
- new net V_BATT2: C30.1, C32.1, C33.1, D5.C, J3.72, R20.2, U7.VDD@36, U7.VDD@37, U9.2
- new net V_BATT3: C41.1, C43.1, C44.1, D8.C, J4.72, R29.2, U10.VDD@36, U10.VDD@37, U12.2
- new net V_BATT4: C52.1, C54.1, C55.1, D10.C, J5.72, R38.2, U13.VDD@36, U13.VDD@37, U15.2
- new net V_BATT5: C63.1, C65.1, C66.1, D12.C, J6.72, R47.2, U16.VDD@36, U16.VDD@37, U18.2
- new net V_BATT6: C74.1, C76.1, C77.1, D14.C, J7.72, R56.2, U19.VDD@36, U19.VDD@37, U21.2
- new net V_BATT7: C85.1, C87.1, C88.1, D16.C, J8.72, R65.2, U22.VDD@36, U22.VDD@37, U24.2
- new net V_BATT8: C96.1, C98.1, C99.1, D18.C, J9.72, R74.2, U25.VDD@36, U25.VDD@37, U27.2
- new net V_BATT9: C107.1, C109.1, C110.1, D20.C, J10.72, R83.2, U28.VDD@36, U28.VDD@37, U30.2
- net 3.3V: now also D7.A, J1.2, J1.74; no longer C1.1, C3.1, C4.1, D7.C, J1.72, R14.2, U1.VDD@36, U1.VDD@37, U2.2
- net 3.3V1: now also D3.A, J2.2, J2.74; no longer C14.1, C16.1, C19.1, D3.C, J2.72, R9.2, U3.VDD@36, U3.VDD@37, U5.2
- net 3.3V10: now also D22.A, J11.2, J11.74; no longer C118.1, C120.1, C121.1, D22.C, J11.72, R92.2, U31.VDD@36, U31.VDD@37, U33.2
- net 3.3V11: now also D24.A, J12.2, J12.74; no longer C129.1, C131.1, C132.1, D24.C, J12.72, R101.2, U34.VDD@36, U34.VDD@37, U36.2
- net 3.3V12: now also D26.A, J13.2, J13.74; no longer C140.1, C142.1, C143.1, D26.C, J13.72, R110.2, U37.VDD@36, U37.VDD@37, U39.2
- net 3.3V13: now also D28.A, J14.2, J14.74; no longer C151.1, C153.1, C154.1, D28.C, J14.72, R119.2, U40.VDD@36, U40.VDD@37, U42.2
- net 3.3V14: now also D30.A, J15.2, J15.74; no longer C162.1, C164.1, C165.1, D30.C, J15.72, R128.2, U43.VDD@36, U43.VDD@37, U45.2
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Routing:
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- added copper zone on layer 15, net V_BATT
- added copper zone on layer 15, net V_BATT1
- added copper zone on layer 15, net V_BATT10
- added copper zone on layer 15, net V_BATT11
- added copper zone on layer 15, net V_BATT12
- added copper zone on layer 15, net V_BATT13
- added copper zone on layer 15, net V_BATT14
- added copper zone on layer 15, net V_BATT15
- added copper zone on layer 15, net V_BATT2
- added copper zone on layer 15, net V_BATT3
- added copper zone on layer 15, net V_BATT4
- added copper zone on layer 15, net V_BATT5
- added copper zone on layer 15, net V_BATT6
- added copper zone on layer 15, net V_BATT7
- added copper zone on layer 15, net V_BATT8
- added copper zone on layer 15, net V_BATT9
- removed copper zone on layer 15, net 3.3V
- removed copper zone on layer 15, net 3.3V1
- removed copper zone on layer 15, net 3.3V10
- removed copper zone on layer 15, net 3.3V11
- removed copper zone on layer 15, net 3.3V12
- removed copper zone on layer 15, net 3.3V13
- removed copper zone on layer 15, net 3.3V14
- removed copper zone on layer 15, net 3.3V15
- removed copper zone on layer 15, net 3.3V2
- removed copper zone on layer 15, net 3.3V3
- removed copper zone on layer 15, net 3.3V4
- removed copper zone on layer 15, net 3.3V5
- removed copper zone on layer 15, net 3.3V6
- removed copper zone on layer 15, net 3.3V7
- removed copper zone on layer 15, net 3.3V8
- removed copper zone on layer 15, net 3.3V9
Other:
- board text added: "v17"
- board text removed: "v16"
